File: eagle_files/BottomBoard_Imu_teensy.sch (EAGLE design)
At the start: 41 parts, among them K1 MK20DX256VLH7, K2 MKL04Z32VLC4, T1 MCP1825S, U1 52207-0885, U2 MPU-9250

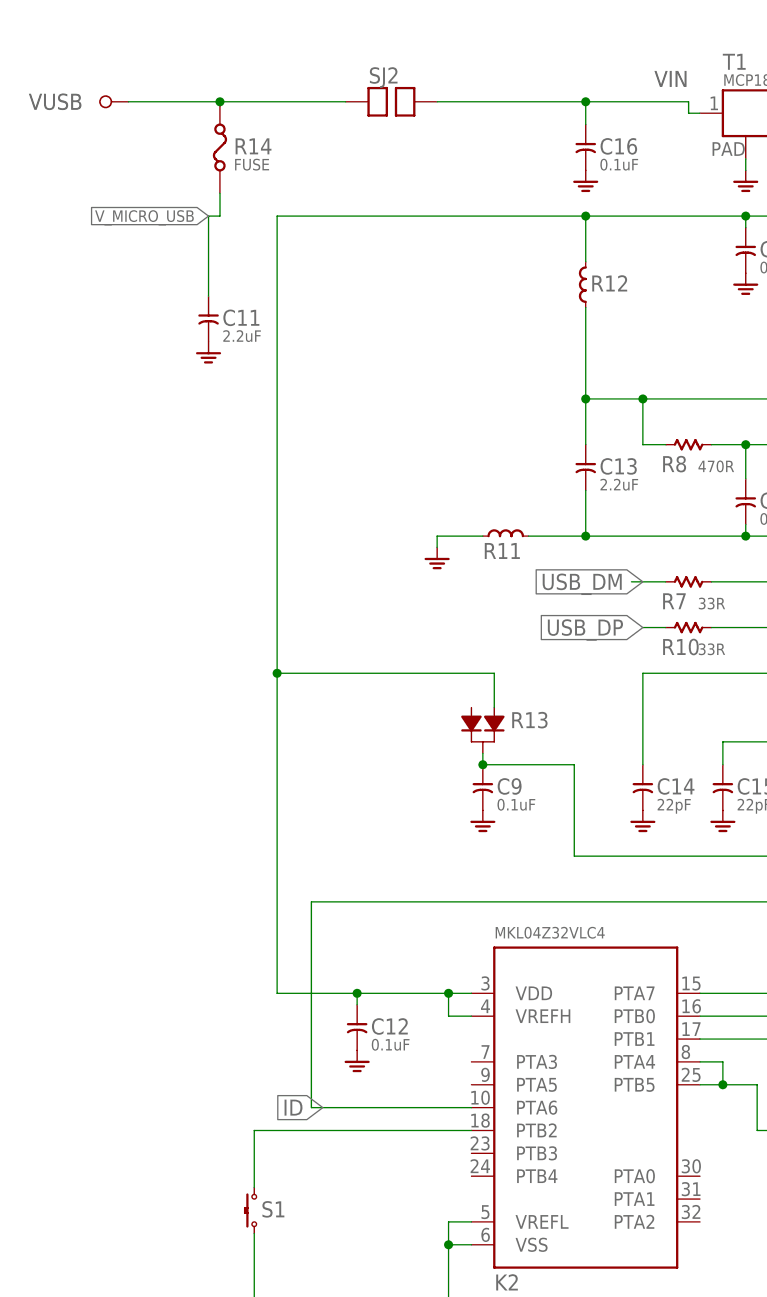
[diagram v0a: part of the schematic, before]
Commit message: top layer board routing
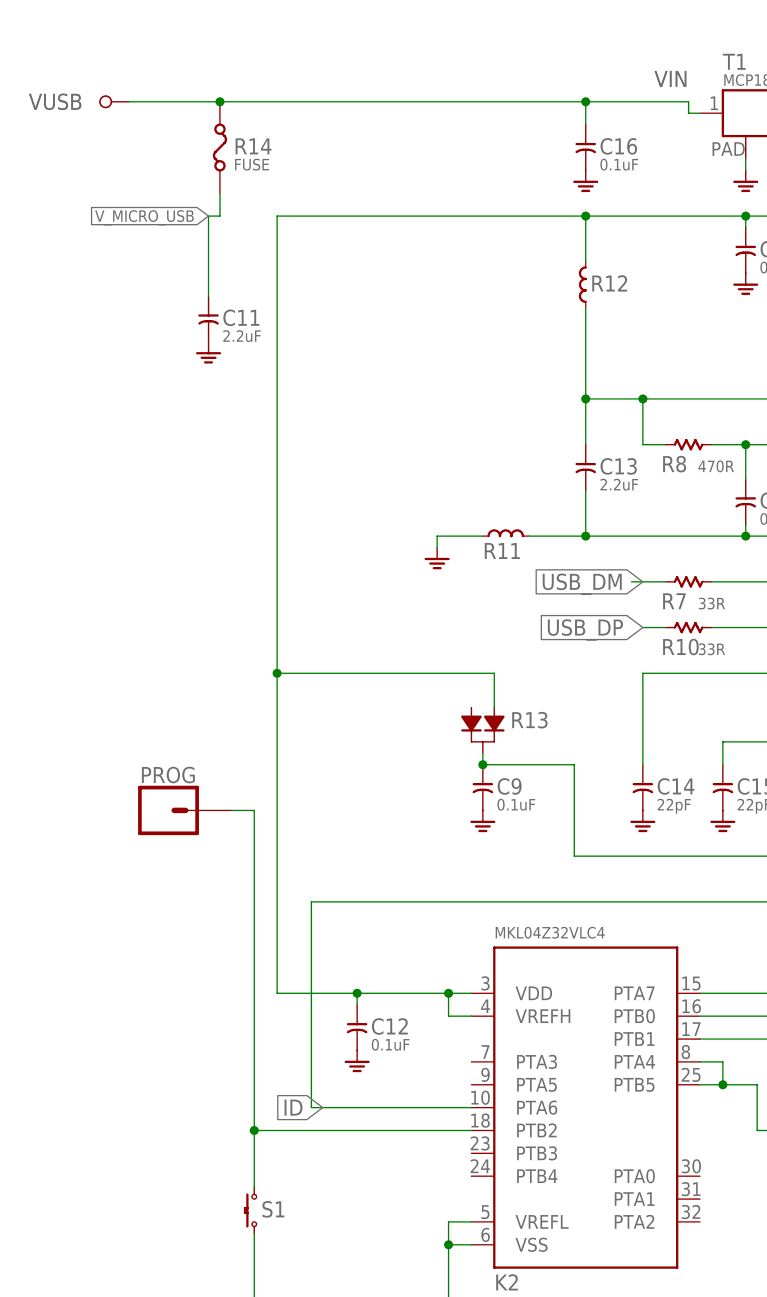
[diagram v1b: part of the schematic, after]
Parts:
- removed SJ2: (no value), t32_ref:SOLDERJUMPER
- added PROG: (no value), SparkFun-Connectors:CONN_01PTH_2MM
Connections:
- removed net N$61: C16.1, SJ2.2, T1.IN
- net N$67: now also C16.1, T1.IN; no longer SJ2.1
- net N$9: now also PROG.1
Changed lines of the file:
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@@
 <part name="S1" library="t32_ref" deviceset="TACT_SWITCH" device=""/>
 <part name="GND28" library="t32_ref" deviceset="GND" device=""/>
-<part name="SJ2" library="t32_ref" deviceset="SOLDERJUMPER" device=""/>
 <part name="R14" library="t32_ref" deviceset="FUSE" device="" value="FUSE"/>
 <part name="C16" library="t32_ref" deviceset="CAPACITOR-0.1UF" device="" value="0.1uF"/>
@@
 <part name="GND30" library="SparkFun-PowerSymbols" library_urn="urn:adsk.eagle:library:530" deviceset="GND" device=""/>
 <part name="CAM_MOLEX" library="con-molex" deviceset="22-23-2041" device=""/>
+<part name="PROG" library="SparkFun-Connectors" library_urn="urn:adsk.eagle:library:513" deviceset="CONN_01" device="PTH_2MM" package3d_urn="urn:adsk.eagle:package:38029/1"/>
 </parts>
 <sheets>
@@
 </instance>
 <instance part="GND28" gate="1" x="-63.5" y="-27.94" smashed="yes"/>
-<instance part="SJ2" gate="G$1" x="-48.26" y="106.68" smashed="yes">
-<attribute name="NAME" x="-50.8" y="108.712" size="1.778" layer="95"/>
-</instance>
 <instance part="R14" gate="G$1" x="-67.31" y="101.6" smashed="yes" rot="R90">
 <attribute name="NAME" x="-65.786" y="100.838" size="1.778" layer="95" ratio="10"/>
@@
 <instance part="CAM_MOLEX" gate="-4" x="40.64" y="-50.8" smashed="yes">
 <attribute name="NAME" x="43.18" y="-51.562" size="1.524" layer="95"/>
+</instance>
+<instance part="PROG" gate="G$1" x="-73.66" y="27.94" smashed="yes">
+<attribute name="VALUE" x="-76.2" y="23.114" size="1.778" layer="96" font="vector"/>
+<attribute name="NAME" x="-76.2" y="30.988" size="1.778" layer="95" font="vector"/>
 </instance>
 </instances>
@@
 </segment>
 </net>
-<net name="N$61" class="0">
-<segment>
+<net name="N$9" class="0">
+<segment>
+<pinref part="K2" gate="G$1" pin="PTB2"/>
+<wire x1="-39.37" y1="-7.62" x2="-63.5" y2="-7.62" width="0.1524" layer="91"/>
+<pinref part="S1" gate="G$1" pin="1"/>
+<wire x1="-63.5" y1="-13.97" x2="-63.5" y2="-7.62" width="0.1524" layer="91"/>
+<pinref part="PROG" gate="G$1" pin="1"/>
+<wire x1="-63.5" y1="-7.62" x2="-63.5" y2="27.94" width="0.1524" layer="91"/>
+<wire x1="-63.5" y1="27.94" x2="-66.04" y2="27.94" width="0.1524" layer="91"/>
+<junction x="-63.5" y="-7.62"/>
+</segment>
+</net>
+<net name="N$67" class="0">
+<segment>
+<pinref part="SX1" gate="G$1" pin="P$1"/>
+<wire x1="-77.47" y1="106.68" x2="-67.31" y2="106.68" width="0.1524" layer="91"/>
+<pinref part="R14" gate="G$1" pin="2"/>
+<wire x1="-26.67" y1="106.68" x2="-67.31" y2="106.68" width="0.1524" layer="91"/>
+<junction x="-67.31" y="106.68"/>
 <pinref part="T1" gate="G$1" pin="IN"/>
 <wire x1="-13.97" y1="105.41" x2="-15.24" y2="105.41" width="0.1524" layer="91"/>
 <wire x1="-15.24" y1="105.41" x2="-15.24" y2="106.68" width="0.1524" layer="91"/>
 <wire x1="-15.24" y1="106.68" x2="-26.67" y2="106.68" width="0.1524" layer="91"/>
-<pinref part="SJ2" gate="G$1" pin="2"/>
 <pinref part="C16" gate="G$1" pin="1"/>
-<wire x1="-26.67" y1="106.68" x2="-43.18" y2="106.68" width="0.1524" layer="91"/>
 <wire x1="-26.67" y1="104.14" x2="-26.67" y2="106.68" width="0.1524" layer="91"/>
 <junction x="-26.67" y="106.68"/>
 </segment>
 </net>
-<net name="N$9" class="0">
-<segment>
-<pinref part="K2" gate="G$1" pin="PTB2"/>
-<wire x1="-39.37" y1="-7.62" x2="-63.5" y2="-7.62" width="0.1524" layer="91"/>
-<pinref part="S1" gate="G$1" pin="1"/>
-<wire x1="-63.5" y1="-13.97" x2="-63.5" y2="-7.62" width="0.1524" layer="91"/>
-</segment>
-</net>
-<net name="N$67" class="0">
-<segment>
-<pinref part="SX1" gate="G$1" pin="P$1"/>
-<wire x1="-77.47" y1="106.68" x2="-67.31" y2="106.68" width="0.1524" layer="91"/>
-<pinref part="R14" gate="G$1" pin="2"/>
-<pinref part="SJ2" gate="G$1" pin="1"/>
-<wire x1="-53.34" y1="106.68" x2="-67.31" y2="106.68" width="0.1524" layer="91"/>
-<junction x="-67.31" y="106.68"/>
-</segment>
-</net>
